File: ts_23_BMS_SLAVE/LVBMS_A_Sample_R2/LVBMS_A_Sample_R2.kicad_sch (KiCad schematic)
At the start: 61 parts, among them J1 S2B-PH-K-S_LF__SN_, J2 Conn_01x13_Male, J3 S2B-PH-K-S_LF__SN_, J4 Conn_02x05_Counter_Clockwise, Q1 BSS308PE_H6327, Q15 DTC114E, Q2 CZT5551CT-ND, T1 HX1188NL, U1 LTC6811

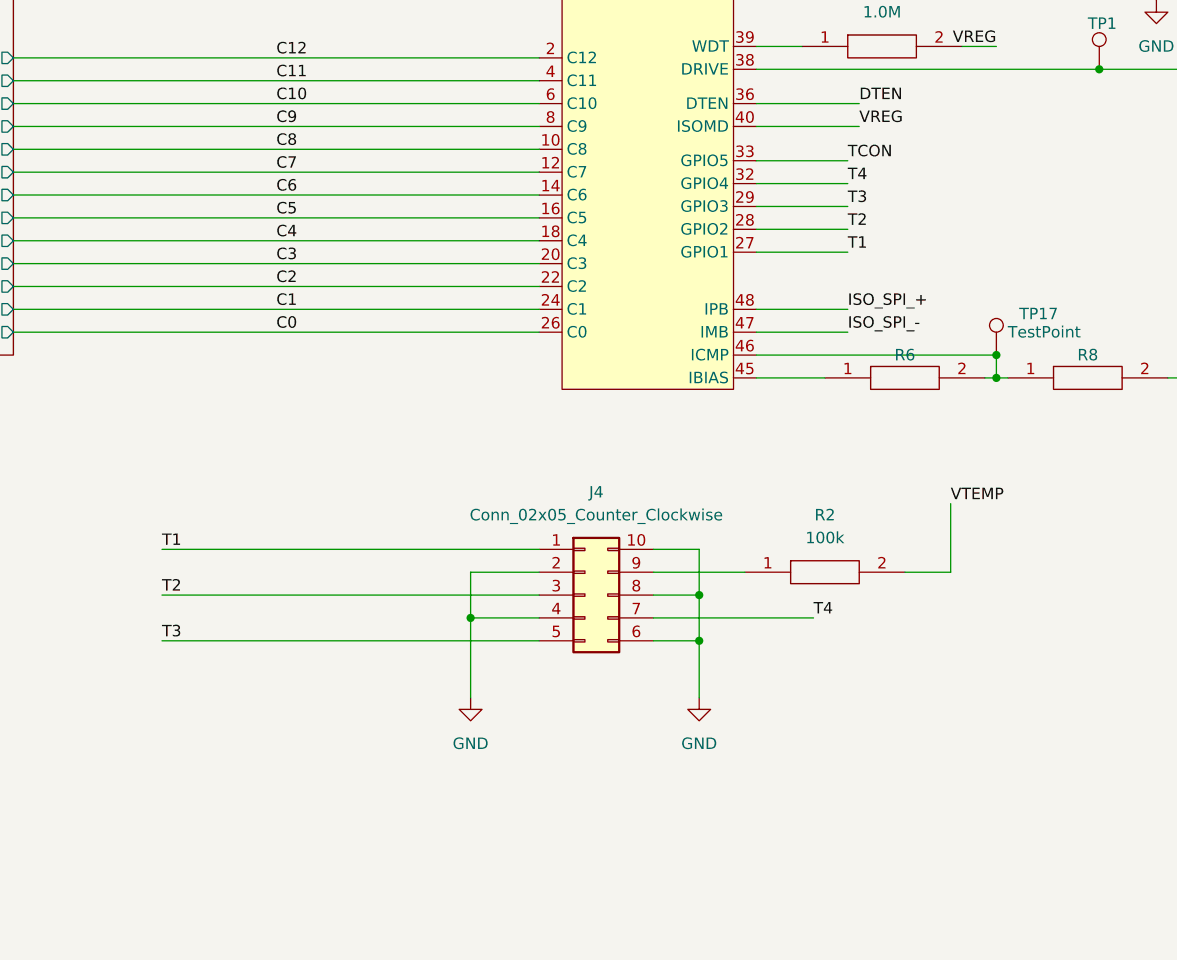
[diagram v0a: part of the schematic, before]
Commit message: LV BMS Updates
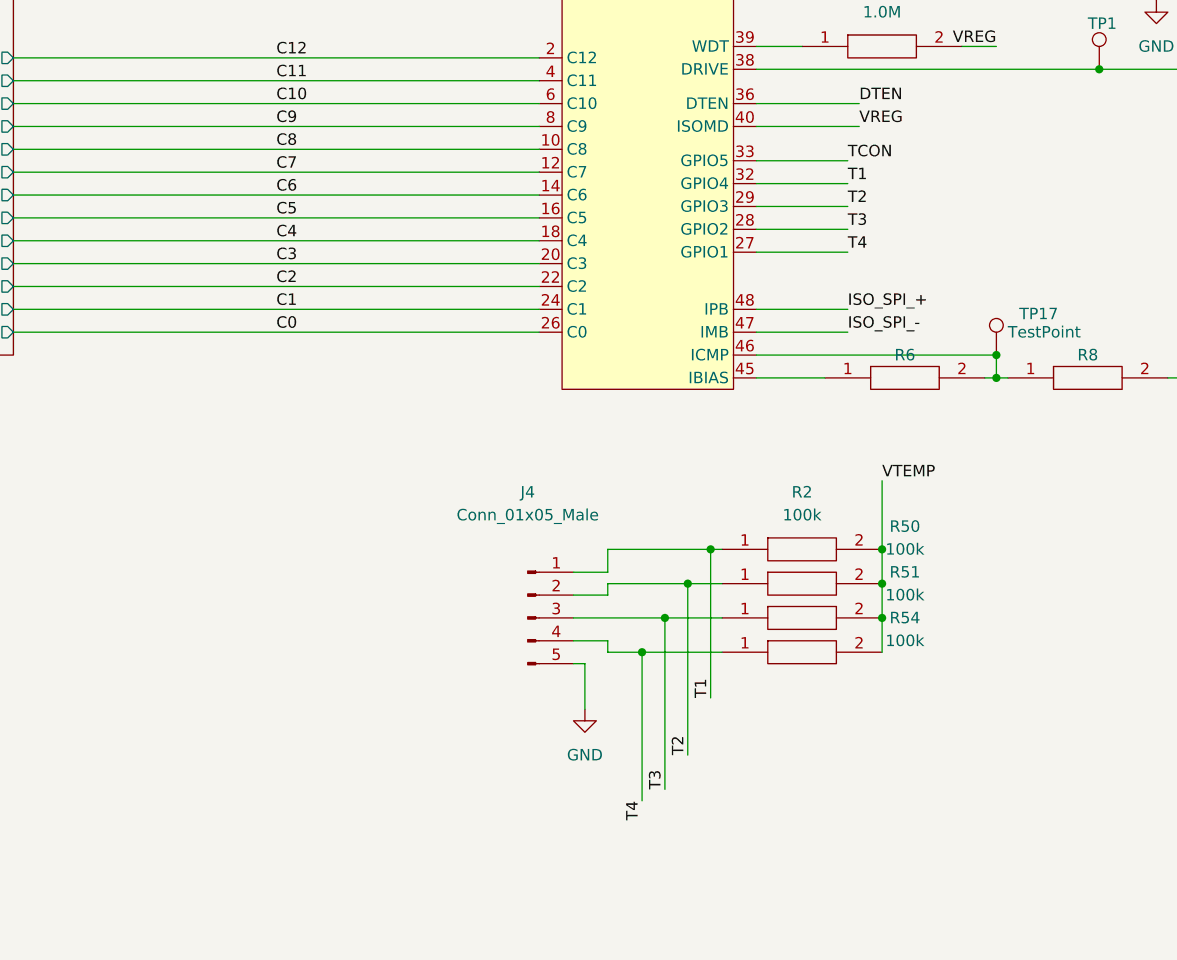
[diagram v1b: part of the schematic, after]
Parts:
- removed J4: Conn_02x05_Counter_Clockwise, Connector_PinSocket_2.54mm:PinSocket_2x05_P2.54mm_Vertical, symbol Connector_Generic:Conn_02x05_Counter_Clockwise
- added J4: Conn_01x05_Male, Connector_PinSocket_2.54mm:PinSocket_1x05_P2.54mm_Vertical, symbol Connector:Conn_01x05_Male
- added R50, R51, R54: 100k, Resistor_SMD:R_0603_1608Metric_Pad0.98x0.95mm_HandSolder, symbol ERJP06F1000V:ERJP06F1000V
- J1, J3: footprint Connector_Molex:Molex_Mini-Fit_Jr_5566-02A_2x01_P4.20mm_Vertical -> Connector_JST:JST_EH_B2B-EH-A_1x02_P2.50mm_Vertical
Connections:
- net GND: now also J4.5 (Pin_5)
- net T1: now also R2.1, U1.32 (GPIO4), J4.1 (Pin_1); no longer U1.27 (GPIO1)
- net T2: now also U1.29 (GPIO3), J4.2 (Pin_2), R50.1; no longer U1.28 (GPIO2)
- net T3: now also U1.28 (GPIO2), J4.3 (Pin_3), R51.1; no longer U1.29 (GPIO3)
- net T4: now also U1.27 (GPIO1), J4.4 (Pin_4), R54.1; no longer U1.32 (GPIO4)
- net VTEMP: now also R50.2, R51.2, R54.2
